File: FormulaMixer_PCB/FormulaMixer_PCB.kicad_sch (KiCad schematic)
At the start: 43 parts, among them J1 Conn_01x04, J2 Conn_01x04, J3 Conn_01x04, J4 Conn_01x04, J5 Conn_01x02, Q1 BC847, Q2 BC847, SW1 RotaryEncoder_Switch, SW2 SW_Push, SW3 SW_Push, U1 74HCT237, U10 BD62130AEFJ, U11 BD62130AEFJ, U12 MC78M05_TO252, U2 74HCT237, U3 BD62130AEFJ, U4 BD62130AEFJ, U5 BD62130AEFJ, U6 BD62130AEFJ, U7 LCD-016N002L, U8 BD62130AEFJ, U9 BD62130AEFJ

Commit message: Add external pullups to encoder output
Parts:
- added R7, R8: 10k, Resistor_SMD:R_0603_1608Metric, symbol Device:R_Small_US
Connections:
- net +3V3: now also R7.1, R8.2
- net ENC_A: now also R7.2
- net ENC_B: now also R8.1
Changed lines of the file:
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@@
   (junction (at 79.502 78.74) (diameter 0) (color 0 0 0 0)
   )
+  (junction (at 19.304 29.21) (diameter 0) (color 0 0 0 0)
+  )
   (junction (at 27.686 153.924) (diameter 0) (color 0 0 0 0)
   )
@@
   (junction (at 138.176 149.606) (diameter 0) (color 0 0 0 0)
   )
+  (junction (at 20.32 21.59) (diameter 0) (color 0 0 0 0)
+  )
   (junction (at 271.018 128.27) (diameter 0) (color 0 0 0 0)
   )
@@
     (stroke (width 0) (type default) (color 0 0 0 0))
   )
+  (wire (pts (xy 21.336 21.59) (xy 20.32 21.59))
+    (stroke (width 0) (type default) (color 0 0 0 0))
+  )
   (polyline (pts (xy 20.574 90.424) (xy 58.42 90.424))
     (stroke (width 0) (type default) (color 0 0 0 0))
@@
     (stroke (width 0) (type default) (color 0 0 0 0))
   )
+  (wire (pts (xy 21.59 36.83) (xy 19.304 36.83))
+    (stroke (width 0) (type default) (color 0 0 0 0))
+  )
   (wire (pts (xy 175.514 162.306) (xy 183.896 162.306))
     (stroke (width 0) (type default) (color 0 0 0 0))
@@
     (stroke (width 0) (type default) (color 0 0 0 0))
   )
+  (wire (pts (xy 19.304 29.21) (xy 19.304 21.59))
+    (stroke (width 0) (type default) (color 0 0 0 0))
+  )
   (wire (pts (xy 175.514 121.666) (xy 183.896 121.666))
     (stroke (width 0) (type default) (color 0 0 0 0))
@@
     (stroke (width 0) (type default) (color 0 0 0 0))
   )
-  (wire (pts (xy 23.622 26.67) (xy 29.21 26.67))
-    (stroke (width 0) (type default) (color 0 0 0 0))
-  )
   (wire (pts (xy 72.136 144.272) (xy 81.28 144.272))
     (stroke (width 0) (type default) (color 0 0 0 0))
@@
     (stroke (width 0) (type default) (color 0 0 0 0))
   )
+  (wire (pts (xy 19.304 36.83) (xy 19.304 29.21))
+    (stroke (width 0) (type default) (color 0 0 0 0))
+  )
   (wire (pts (xy 48.006 159.004) (xy 50.292 159.004))
     (stroke (width 0) (type default) (color 0 0 0 0))
@@
     (stroke (width 0) (type default) (color 0 0 0 0))
   )
-  (wire (pts (xy 19.558 29.21) (xy 29.21 29.21))
+  (wire (pts (xy 19.304 29.21) (xy 29.21 29.21))
     (stroke (width 0) (type default) (color 0 0 0 0))
   )
@@
     (stroke (width 0) (type default) (color 0 0 0 0))
   )
-  (wire (pts (xy 23.622 31.75) (xy 29.21 31.75))
+  (wire (pts (xy 21.59 31.75) (xy 29.21 31.75))
     (stroke (width 0) (type default) (color 0 0 0 0))
   )
@@
     (stroke (width 0) (type default) (color 0 0 0 0))
   )
+  (wire (pts (xy 19.304 21.59) (xy 20.32 21.59))
+    (stroke (width 0) (type default) (color 0 0 0 0))
+  )
   (wire (pts (xy 128.016 170.942) (xy 128.016 173.482))
     (stroke (width 0) (type default) (color 0 0 0 0))
@@
     (stroke (width 0) (type default) (color 0 0 0 0))
   )
+  (wire (pts (xy 21.336 26.67) (xy 29.21 26.67))
+    (stroke (width 0) (type default) (color 0 0 0 0))
+  )
   (wire (pts (xy 72.136 84.074) (xy 80.01 84.074))
     (stroke (width 0) (type default) (color 0 0 0 0))
@@
     (pin "2")
   )
+  (symbol (lib_id "Device:R_Small_US") (at 21.336 24.13 0) (unit 1)
+    (in_bom yes) (on_board yes)
+    (property "Reference" "R7" (id 0) (at 22.606 21.844 0)
+      (effects (font (size 1.27 1.27)) (justify left))
+    )
+    (property "Value" "10k" (id 1) (at 22.606 23.622 0)
+      (effects (font (size 1.27 1.27)) (justify left))
+    )
+    (property "Footprint" "Resistor_SMD:R_0603_1608Metric" (id 2) (at 21.336 24.13 0)
+      (effects (font (size 1.27 1.27)) hide)
+    )
+    (property "Datasheet" "~" (id 3) (at 21.336 24.13 0)
+      (effects (font (size 1.27 1.27)) hide)
+    )
+    (pin "1")
+    (pin "2")
+  )
   (symbol (lib_id "power:GND") (at 65.532 41.91 0) (unit 1)
     (in_bom yes) (on_board yes)
@@
     (pin "1")
   )
+  (symbol (lib_id "Device:R_Small_US") (at 21.59 34.29 0) (unit 1)
+    (in_bom yes) (on_board yes)
+    (property "Reference" "R8" (id 0) (at 23.114 34.036 0)
+      (effects (font (size 1.27 1.27)) (justify left))
+    )
+    (property "Value" "10k" (id 1) (at 22.86 35.814 0)
+      (effects (font (size 1.27 1.27)) (justify left))
+    )
+    (property "Footprint" "Resistor_SMD:R_0603_1608Metric" (id 2) (at 21.59 34.29 0)
+      (effects (font (size 1.27 1.27)) hide)
+    )
+    (property "Datasheet" "~" (id 3) (at 21.59 34.29 0)
+      (effects (font (size 1.27 1.27)) hide)
+    )
+    (pin "1")
+    (pin "2")
+  )
   (symbol (lib_id "power:+3.3V") (at 50.546 20.828 0) (unit 1)
     (in_bom yes) (on_board yes)
@@
     (pin "2")
   )
-  (symbol (lib_id "power:+3.3V") (at 19.558 29.21 0) (unit 1)
-    (in_bom yes) (on_board yes) (fields_autoplaced)
-    (property "Reference" "#PWR01" (id 0) (at 19.558 33.02 0)
+  (symbol (lib_id "power:+3.3V") (at 20.32 21.59 0) (unit 1)
+    (in_bom yes) (on_board yes)
+    (property "Reference" "#PWR01" (id 0) (at 20.32 25.4 0)
       (effects (font (size 1.27 1.27)) hide)
     )
-    (property "Value" "+3.3V" (id 1) (at 19.558 23.622 0))
-    (property "Footprint" "" (id 2) (at 19.558 29.21 0)
+    (property "Value" "+3.3V" (id 1) (at 20.32 18.288 0))
+    (property "Footprint" "" (id 2) (at 20.32 21.59 0)
       (effects (font (size 1.27 1.27)) hide)
     )
-    (property "Datasheet" "" (id 3) (at 19.558 29.21 0)
+    (property "Datasheet" "" (id 3) (at 20.32 21.59 0)
       (effects (font (size 1.27 1.27)) hide)
     )
@@
       (reference "R6") (unit 1) (value "10k") (footprint "Resistor_SMD:R_0603_1608Metric")
     )
+    (path "/2e15a928-960d-40bd-bb99-4419ff498b6b"
+      (reference "R7") (unit 1) (value "10k") (footprint "Resistor_SMD:R_0603_1608Metric")
+    )
+    (path "/98156482-3249-4efa-b63a-d02c36050f56"
+      (reference "R8") (unit 1) (value "10k") (footprint "Resistor_SMD:R_0603_1608Metric")
+    )
     (path "/650b219e-4733-4d5d-b75e-c3a543c4b045"

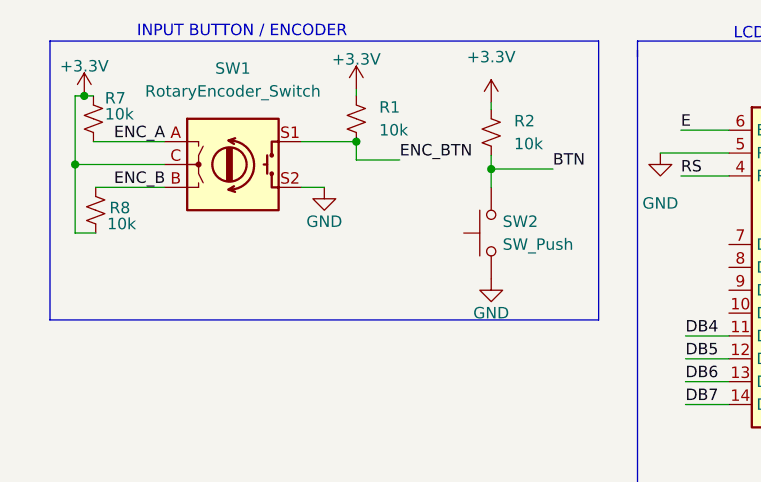
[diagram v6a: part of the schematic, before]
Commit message: Ope those are suppose to be pulldowns
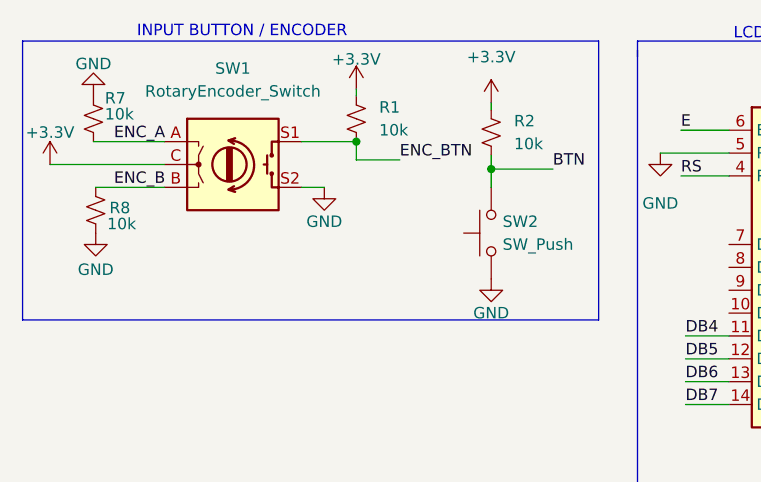
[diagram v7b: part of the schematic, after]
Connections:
- net +3V3: no longer R7.1, R8.2
- net GND: now also R7.1, R8.2
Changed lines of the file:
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@@
   (junction (at 79.502 78.74) (diameter 0) (color 0 0 0 0)
   )
-  (junction (at 19.304 29.21) (diameter 0) (color 0 0 0 0)
-  )
   (junction (at 27.686 153.924) (diameter 0) (color 0 0 0 0)
   )
@@
   (junction (at 138.176 149.606) (diameter 0) (color 0 0 0 0)
   )
-  (junction (at 20.32 21.59) (diameter 0) (color 0 0 0 0)
-  )
   (junction (at 271.018 128.27) (diameter 0) (color 0 0 0 0)
   )
@@
     (stroke (width 0) (type default) (color 0 0 0 0))
   )
-  (wire (pts (xy 21.336 21.59) (xy 20.32 21.59))
-    (stroke (width 0) (type default) (color 0 0 0 0))
-  )
   (polyline (pts (xy 20.574 90.424) (xy 58.42 90.424))
     (stroke (width 0) (type default) (color 0 0 0 0))
@@
     (stroke (width 0) (type default) (color 0 0 0 0))
   )
-  (wire (pts (xy 21.59 36.83) (xy 19.304 36.83))
-    (stroke (width 0) (type default) (color 0 0 0 0))
-  )
   (wire (pts (xy 175.514 162.306) (xy 183.896 162.306))
     (stroke (width 0) (type default) (color 0 0 0 0))
@@
     (stroke (width 0) (type default) (color 0 0 0 0))
   )
-  (wire (pts (xy 19.304 29.21) (xy 19.304 21.59))
-    (stroke (width 0) (type default) (color 0 0 0 0))
-  )
   (wire (pts (xy 175.514 121.666) (xy 183.896 121.666))
     (stroke (width 0) (type default) (color 0 0 0 0))
@@
     (stroke (width 0) (type default) (color 0 0 0 0))
   )
-  (polyline (pts (xy 16.51 15.494) (xy 77.47 15.494))
-    (stroke (width 0) (type default) (color 0 0 0 0))
-  )
-  (wire (pts (xy 19.304 36.83) (xy 19.304 29.21))
+  (polyline (pts (xy 13.462 15.494) (xy 77.47 15.494))
     (stroke (width 0) (type default) (color 0 0 0 0))
   )
@@
     (stroke (width 0) (type default) (color 0 0 0 0))
   )
-  (wire (pts (xy 19.304 29.21) (xy 29.21 29.21))
+  (wire (pts (xy 16.51 29.21) (xy 29.21 29.21))
     (stroke (width 0) (type default) (color 0 0 0 0))
   )
@@
     (stroke (width 0) (type default) (color 0 0 0 0))
   )
-  (polyline (pts (xy 77.47 46.482) (xy 16.51 46.482))
+  (polyline (pts (xy 77.47 46.482) (xy 13.462 46.482))
     (stroke (width 0) (type default) (color 0 0 0 0))
   )
@@
     (stroke (width 0) (type default) (color 0 0 0 0))
   )
-  (polyline (pts (xy 16.51 46.482) (xy 16.51 15.494))
+  (polyline (pts (xy 13.462 46.482) (xy 13.462 15.494))
     (stroke (width 0) (type default) (color 0 0 0 0))
   )
@@
     (stroke (width 0) (type default) (color 0 0 0 0))
   )
-  (wire (pts (xy 19.304 21.59) (xy 20.32 21.59))
-    (stroke (width 0) (type default) (color 0 0 0 0))
-  )
   (wire (pts (xy 128.016 170.942) (xy 128.016 173.482))
     (stroke (width 0) (type default) (color 0 0 0 0))
@@
     (pin "2")
   )
+  (symbol (lib_id "power:GND") (at 21.336 21.59 180) (unit 1)
+    (in_bom yes) (on_board yes)
+    (property "Reference" "#PWR?" (id 0) (at 21.336 15.24 0)
+      (effects (font (size 1.27 1.27)) hide)
+    )
+    (property "Value" "GND" (id 1) (at 21.336 18.034 0))
+    (property "Footprint" "" (id 2) (at 21.336 21.59 0)
+      (effects (font (size 1.27 1.27)) hide)
+    )
+    (property "Datasheet" "" (id 3) (at 21.336 21.59 0)
+      (effects (font (size 1.27 1.27)) hide)
+    )
+    (pin "1")
+  )
   (symbol (lib_id "power:GND") (at 65.532 41.91 0) (unit 1)
     (in_bom yes) (on_board yes)
@@
     (pin "1")
   )
+  (symbol (lib_id "power:GND") (at 21.59 36.83 0) (unit 1)
+    (in_bom yes) (on_board yes)
+    (property "Reference" "#PWR?" (id 0) (at 21.59 43.18 0)
+      (effects (font (size 1.27 1.27)) hide)
+    )
+    (property "Value" "GND" (id 1) (at 21.59 40.894 0))
+    (property "Footprint" "" (id 2) (at 21.59 36.83 0)
+      (effects (font (size 1.27 1.27)) hide)
+    )
+    (property "Datasheet" "" (id 3) (at 21.59 36.83 0)
+      (effects (font (size 1.27 1.27)) hide)
+    )
+    (pin "1")
+  )
   (symbol (lib_id "Switch:SW_Push") (at 65.532 36.83 90) (unit 1)
     (in_bom yes) (on_board yes) (fields_autoplaced)
@@
     (pin "1")
   )
+  (symbol (lib_id "power:+3.3V") (at 16.51 29.21 0) (unit 1)
+    (in_bom yes) (on_board yes)
+    (property "Reference" "#PWR?" (id 0) (at 16.51 33.02 0)
+      (effects (font (size 1.27 1.27)) hide)
+    )
+    (property "Value" "+3.3V" (id 1) (at 16.51 25.654 0))
+    (property "Footprint" "" (id 2) (at 16.51 29.21 0)
+      (effects (font (size 1.27 1.27)) hide)
+    )
+    (property "Datasheet" "" (id 3) (at 16.51 29.21 0)
+      (effects (font (size 1.27 1.27)) hide)
+    )
+    (pin "1")
+  )
   (symbol (lib_id "power:+12V") (at 126.238 107.95 0) (unit 1)
     (in_bom yes) (on_board yes)
@@
     (pin "2")
   )
-  (symbol (lib_id "power:+3.3V") (at 20.32 21.59 0) (unit 1)
-    (in_bom yes) (on_board yes)
-    (property "Reference" "#PWR01" (id 0) (at 20.32 25.4 0)
-      (effects (font (size 1.27 1.27)) hide)
-    )
-    (property "Value" "+3.3V" (id 1) (at 20.32 18.288 0))
-    (property "Footprint" "" (id 2) (at 20.32 21.59 0)
-      (effects (font (size 1.27 1.27)) hide)
-    )
-    (property "Datasheet" "" (id 3) (at 20.32 21.59 0)
-      (effects (font (size 1.27 1.27)) hide)
-    )
-    (pin "1")
-  )
   (symbol (lib_id "power:+5V") (at 217.932 27.94 0) (unit 1)
     (in_bom yes) (on_board yes) (fields_autoplaced)
@@
   )
   (symbol_instances
-    (path "/d6cf5cf6-ba04-4da1-ae85-f03cf35b921b"
-      (reference "#PWR01") (unit 1) (value "+3.3V") (footprint "")
-    )
     (path "/8a2920a4-01fe-4d87-a6ee-665fc74c2713"
       (reference "#PWR02") (unit 1) (value "GND") (footprint "")
@@
       (reference "#PWR0102") (unit 1) (value "GND") (footprint "")
     )
+    (path "/2f0b3879-b7da-4bc5-8f4b-299fe53b1a42"
+      (reference "#PWR?") (unit 1) (value "GND") (footprint "")
+    )
+    (path "/742741e4-75d4-4f70-8913-bd0c762eb3a5"
+      (reference "#PWR?") (unit 1) (value "GND") (footprint "")
+    )
+    (path "/824fa6cd-98a9-48b1-a293-af833136a90c"
+      (reference "#PWR?") (unit 1) (value "+3.3V") (footprint "")
+    )
     (path "/fa4b01be-7f14-43c6-b8c2-4fefa331de66"

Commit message: Layout board
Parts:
- U10, U11, U3, U4, U5, U6, U8, U9: footprint Package_SO:SOIC-8-1EP_3.9x4.9mm_P1.27mm_EP2.514x3.2mm_ThermalVias -> Package_SO:SOIC-8-1EP_3.9x4.9mm_P1.27mm_EP2.514x3.2mm
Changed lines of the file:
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@@
   (symbol (lib_id "power:GND") (at 21.336 21.59 180) (unit 1)
     (in_bom yes) (on_board yes)
-    (property "Reference" "#PWR?" (id 0) (at 21.336 15.24 0)
+    (property "Reference" "#PWR0104" (id 0) (at 21.336 15.24 0)
       (effects (font (size 1.27 1.27)) hide)
     )
@@
     (property "Reference" "U10" (id 0) (at 138.303 129.54 0))
     (property "Value" "BD62130AEFJ" (id 1) (at 138.303 132.08 0))
-    (property "Footprint" "Package_SO:SOIC-8-1EP_3.9x4.9mm_P1.27mm_EP2.514x3.2mm_ThermalVias" (id 2) (at 138.303 147.955 0)
+    (property "Footprint" "Package_SO:SOIC-8-1EP_3.9x4.9mm_P1.27mm_EP2.514x3.2mm" (id 2) (at 138.303 147.955 0)
       (effects (font (size 1.27 1.27)) hide)
     )
@@
   (symbol (lib_id "power:GND") (at 21.59 36.83 0) (unit 1)
     (in_bom yes) (on_board yes)
-    (property "Reference" "#PWR?" (id 0) (at 21.59 43.18 0)
+    (property "Reference" "#PWR0105" (id 0) (at 21.59 43.18 0)
       (effects (font (size 1.27 1.27)) hide)
     )
@@
   (symbol (lib_id "power:+3.3V") (at 16.51 29.21 0) (unit 1)
     (in_bom yes) (on_board yes)
-    (property "Reference" "#PWR?" (id 0) (at 16.51 33.02 0)
+    (property "Reference" "#PWR0103" (id 0) (at 16.51 33.02 0)
       (effects (font (size 1.27 1.27)) hide)
     )
@@
     (property "Reference" "U4" (id 0) (at 91.567 101.6 0))
     (property "Value" "BD62130AEFJ" (id 1) (at 91.567 104.14 0))
-    (property "Footprint" "Package_SO:SOIC-8-1EP_3.9x4.9mm_P1.27mm_EP2.514x3.2mm_ThermalVias" (id 2) (at 91.567 120.015 0)
+    (property "Footprint" "Package_SO:SOIC-8-1EP_3.9x4.9mm_P1.27mm_EP2.514x3.2mm" (id 2) (at 91.567 120.015 0)
       (effects (font (size 1.27 1.27)) hide)
     )
@@
     (property "Reference" "U8" (id 0) (at 138.049 72.136 0))
     (property "Value" "BD62130AEFJ" (id 1) (at 138.049 74.676 0))
-    (property "Footprint" "Package_SO:SOIC-8-1EP_3.9x4.9mm_P1.27mm_EP2.514x3.2mm_ThermalVias" (id 2) (at 138.049 90.551 0)
+    (property "Footprint" "Package_SO:SOIC-8-1EP_3.9x4.9mm_P1.27mm_EP2.514x3.2mm" (id 2) (at 138.049 90.551 0)
       (effects (font (size 1.27 1.27)) hide)
     )
@@
     (property "Reference" "U6" (id 0) (at 91.821 159.258 0))
     (property "Value" "BD62130AEFJ" (id 1) (at 91.821 161.798 0))
-    (property "Footprint" "Package_SO:SOIC-8-1EP_3.9x4.9mm_P1.27mm_EP2.514x3.2mm_ThermalVias" (id 2) (at 91.821 177.673 0)
+    (property "Footprint" "Package_SO:SOIC-8-1EP_3.9x4.9mm_P1.27mm_EP2.514x3.2mm" (id 2) (at 91.821 177.673 0)
       (effects (font (size 1.27 1.27)) hide)
     )
@@
     (property "Reference" "U5" (id 0) (at 91.567 129.794 0))
     (property "Value" "BD62130AEFJ" (id 1) (at 91.567 132.334 0))
-    (property "Footprint" "Package_SO:SOIC-8-1EP_3.9x4.9mm_P1.27mm_EP2.514x3.2mm_ThermalVias" (id 2) (at 91.567 148.209 0)
+    (property "Footprint" "Package_SO:SOIC-8-1EP_3.9x4.9mm_P1.27mm_EP2.514x3.2mm" (id 2) (at 91.567 148.209 0)
       (effects (font (size 1.27 1.27)) hide)
     )
@@
     (property "Reference" "U3" (id 0) (at 91.567 72.136 0))
     (property "Value" "BD62130AEFJ" (id 1) (at 91.567 74.676 0))
-    (property "Footprint" "Package_SO:SOIC-8-1EP_3.9x4.9mm_P1.27mm_EP2.514x3.2mm_ThermalVias" (id 2) (at 91.567 90.551 0)
+    (property "Footprint" "Package_SO:SOIC-8-1EP_3.9x4.9mm_P1.27mm_EP2.514x3.2mm" (id 2) (at 91.567 90.551 0)
       (effects (font (size 1.27 1.27)) hide)
     )
@@
     (property "Reference" "U11" (id 0) (at 138.303 159.004 0))
     (property "Value" "BD62130AEFJ" (id 1) (at 138.303 161.544 0))
-    (property "Footprint" "Package_SO:SOIC-8-1EP_3.9x4.9mm_P1.27mm_EP2.514x3.2mm_ThermalVias" (id 2) (at 138.303 177.419 0)
+    (property "Footprint" "Package_SO:SOIC-8-1EP_3.9x4.9mm_P1.27mm_EP2.514x3.2mm" (id 2) (at 138.303 177.419 0)
       (effects (font (size 1.27 1.27)) hide)
     )
@@
     (property "Reference" "U9" (id 0) (at 138.303 101.346 0))
     (property "Value" "BD62130AEFJ" (id 1) (at 138.303 103.886 0))
-    (property "Footprint" "Package_SO:SOIC-8-1EP_3.9x4.9mm_P1.27mm_EP2.514x3.2mm_ThermalVias" (id 2) (at 138.303 119.761 0)
+    (property "Footprint" "Package_SO:SOIC-8-1EP_3.9x4.9mm_P1.27mm_EP2.514x3.2mm" (id 2) (at 138.303 119.761 0)
       (effects (font (size 1.27 1.27)) hide)
     )
@@
       (reference "#PWR0102") (unit 1) (value "GND") (footprint "")
     )
+    (path "/824fa6cd-98a9-48b1-a293-af833136a90c"
+      (reference "#PWR0103") (unit 1) (value "+3.3V") (footprint "")
+    )
     (path "/2f0b3879-b7da-4bc5-8f4b-299fe53b1a42"
-      (reference "#PWR?") (unit 1) (value "GND") (footprint "")
+      (reference "#PWR0104") (unit 1) (value "GND") (footprint "")
     )
     (path "/742741e4-75d4-4f70-8913-bd0c762eb3a5"
-      (reference "#PWR?") (unit 1) (value "GND") (footprint "")
-    )
-    (path "/824fa6cd-98a9-48b1-a293-af833136a90c"
-      (reference "#PWR?") (unit 1) (value "+3.3V") (footprint "")
+      (reference "#PWR0105") (unit 1) (value "GND") (footprint "")
     )
     (path "/fa4b01be-7f14-43c6-b8c2-4fefa331de66"
@@
     )
     (path "/f42ca77d-5aa7-41a0-8a57-c05a91f64495"
-      (reference "U3") (unit 1) (value "BD62130AEFJ") (footprint "Package_SO:SOIC-8-1EP_3.9x4.9mm_P1.27mm_EP2.514x3.2mm_ThermalVias")
+      (reference "U3") (unit 1) (value "BD62130AEFJ") (footprint "Package_SO:SOIC-8-1EP_3.9x4.9mm_P1.27mm_EP2.514x3.2mm")
     )
     (path "/8901d2f5-63e8-4f4b-8dec-30c3e8822442"
-      (reference "U4") (unit 1) (value "BD62130AEFJ") (footprint "Package_SO:SOIC-8-1EP_3.9x4.9mm_P1.27mm_EP2.514x3.2mm_ThermalVias")
+      (reference "U4") (unit 1) (value "BD62130AEFJ") (footprint "Package_SO:SOIC-8-1EP_3.9x4.9mm_P1.27mm_EP2.514x3.2mm")
     )
     (path "/dae34607-faab-4596-8df6-7b544ee49cb1"
-      (reference "U5") (unit 1) (value "BD62130AEFJ") (footprint "Package_SO:SOIC-8-1EP_3.9x4.9mm_P1.27mm_EP2.514x3.2mm_ThermalVias")
+      (reference "U5") (unit 1) (value "BD62130AEFJ") (footprint "Package_SO:SOIC-8-1EP_3.9x4.9mm_P1.27mm_EP2.514x3.2mm")
     )
     (path "/cf7f19a8-7514-45d2-b081-1fa8d4dce0fa"
-      (reference "U6") (unit 1) (value "BD62130AEFJ") (footprint "Package_SO:SOIC-8-1EP_3.9x4.9mm_P1.27mm_EP2.514x3.2mm_ThermalVias")
+      (reference "U6") (unit 1) (value "BD62130AEFJ") (footprint "Package_SO:SOIC-8-1EP_3.9x4.9mm_P1.27mm_EP2.514x3.2mm")
     )
     (path "/1e5f7901-dd03-4533-a2fb-24b6a8c35075"
@@
     )
     (path "/9970b746-68c3-46d7-bacd-2a4754043ea6"
-      (reference "U8") (unit 1) (value "BD62130AEFJ") (footprint "Package_SO:SOIC-8-1EP_3.9x4.9mm_P1.27mm_EP2.514x3.2mm_ThermalVias")
+      (reference "U8") (unit 1) (value "BD62130AEFJ") (footprint "Package_SO:SOIC-8-1EP_3.9x4.9mm_P1.27mm_EP2.514x3.2mm")
     )
     (path "/fbec0c5f-48d2-419d-8091-40d8bba072f2"
-      (reference "U9") (unit 1) (value "BD62130AEFJ") (footprint "Package_SO:SOIC-8-1EP_3.9x4.9mm_P1.27mm_EP2.514x3.2mm_ThermalVias")
+      (reference "U9") (unit 1) (value "BD62130AEFJ") (footprint "Package_SO:SOIC-8-1EP_3.9x4.9mm_P1.27mm_EP2.514x3.2mm")
     )
     (path "/3bea65d6-c8a4-44ee-b9cd-8ae258656f8e"
-      (reference "U10") (unit 1) (value "BD62130AEFJ") (footprint "Package_SO:SOIC-8-1EP_3.9x4.9mm_P1.27mm_EP2.514x3.2mm_ThermalVias")
+      (reference "U10") (unit 1) (value "BD62130AEFJ") (footprint "Package_SO:SOIC-8-1EP_3.9x4.9mm_P1.27mm_EP2.514x3.2mm")
     )
     (path "/fb155bd2-b78b-4f0a-9c92-58403da76612"
-      (reference "U11") (unit 1) (value "BD62130AEFJ") (footprint "Package_SO:SOIC-8-1EP_3.9x4.9mm_P1.27mm_EP2.514x3.2mm_ThermalVias")
+      (reference "U11") (unit 1) (value "BD62130AEFJ") (footprint "Package_SO:SOIC-8-1EP_3.9x4.9mm_P1.27mm_EP2.514x3.2mm")
     )
     (path "/a0c8aed4-8c46-47a4-8f0a-dca12784ea48"
